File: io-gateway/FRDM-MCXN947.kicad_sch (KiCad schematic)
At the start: 12 parts, among them M1 Fan_3pin, U6 MCP9700x-ETT

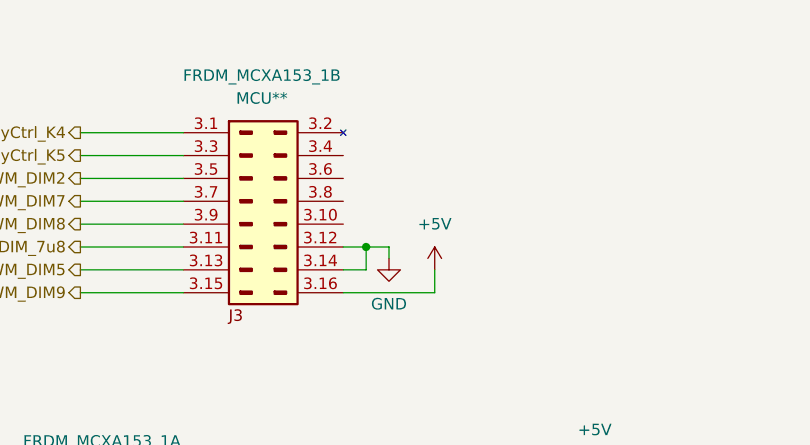
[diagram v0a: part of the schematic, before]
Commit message: Add ESD protection for RS485
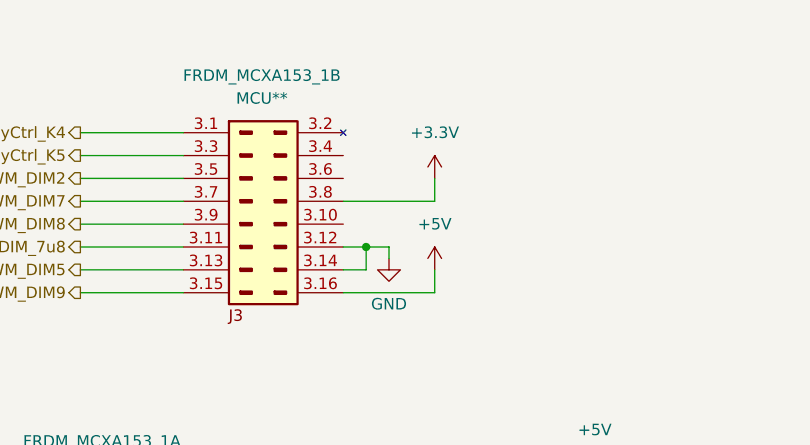
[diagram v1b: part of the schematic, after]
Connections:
- net +3.3V: now reaches FRDM_MCXA153_1.3.8 (Pin_J3_3V3_Out)
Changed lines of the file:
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@@
 	(wire
 		(pts
+			(xy 232.41 82.55) (xy 232.41 85.09)
+		)
+		(stroke
+			(width 0)
+			(type default)
+		)
+	)
+	(wire
+		(pts
 			(xy 266.7 116.84) (xy 250.19 116.84)
 		)
@@
 	(wire
 		(pts
+			(xy 232.41 85.09) (xy 222.25 85.09)
+		)
+		(stroke
+			(width 0)
+			(type default)
+		)
+	)
+	(wire
+		(pts
 			(xy 53.34 80.01) (xy 93.98 80.01)
 		)
@@
 				)
 			)
+		)
+	)
+	(symbol
+		(lib_id "power:+3.3V")
+		(at 232.41 82.55 0)
+		(unit 1)
+		(exclude_from_sim no)
+		(in_bom yes)
+		(on_board yes)
+		(dnp no)
+		(fields_autoplaced yes)
+		(property "Reference" "#PWR078"
+			(at 232.41 86.36 0)
+			(effects
+				(font
+					(size 1.27 1.27)
+				)
+				(hide yes)
+			)
+		)
+		(property "Value" "+3.3V"
+			(at 232.41 77.47 0)
+			(effects
+				(font
+					(size 1.27 1.27)
+				)
+			)
+		)
+		(property "Footprint" ""
+			(at 232.41 82.55 0)
+			(effects
+				(font
+					(size 1.27 1.27)
+				)
+				(hide yes)
+			)
+		)
+		(property "Datasheet" ""
+			(at 232.41 82.55 0)
+			(effects
+				(font
+					(size 1.27 1.27)
+				)
+				(hide yes)
+			)
+		)
+		(property "Description" "Power symbol creates a global label with name \"+3.3V\""
+			(at 232.41 82.55 0)
+			(effects
+				(font
+					(size 1.27 1.27)
+				)
+				(hide yes)
+			)
+		)
+		(pin "1"
+		)
+		(instances
+			(project ""
+				(path "/2cb6f94b-272a-4ed7-b08d-c3630bda6156/f7918fcf-9688-4ae8-a1d7-cb892536f0d4"
+					(reference "#PWR078")
+					(unit 1)
+				)
+			)

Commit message: upd
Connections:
- net RelayCtrl_K8: now also FRDM_MCXA153_1.4.9 (Pin_9); no longer FRDM_MCXA153_1.1.1 (Pin_J1_1)
- net RS485_RTS renamed RS485_DE
- new net RS_485_nRE: FRDM_MCXA153_1.1.1 (Pin_J1_1)
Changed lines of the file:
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@@
+	(wire
+		(pts
+			(xy 166.37 128.27) (xy 176.53 128.27)
+		)
+		(stroke
+			(width 0)
+			(type default)
+		)
+	)
 	(wire
 		(pts
@@
 	(wire
 		(pts
+			(xy 222.25 92.71) (xy 224.79 92.71)
+		)
+		(stroke
+			(width 0)
+			(type default)
+		)
+	)
+	(wire
+		(pts
+			(xy 250.19 133.35) (xy 250.19 135.89)
+		)
+		(stroke
+			(width 0)
+			(type default)
+		)
+	)
+	(wire
+		(pts
+			(xy 92.71 163.83) (xy 92.71 170.18)
+		)
+		(stroke
+			(width 0)
+			(type default)
+		)
+	)
+	(wire
+		(pts
+			(xy 125.73 90.17) (xy 128.27 90.17)
+		)
+		(stroke
+			(width 0)
+			(type default)
+		)
+	)
+	(wire
+		(pts
+			(xy 193.04 87.63) (xy 204.47 87.63)
+		)
+		(stroke
+			(width 0)
+			(type default)
+		)
+	)
+	(wire
+		(pts
+			(xy 40.64 144.78) (xy 40.64 142.24)
+		)
+		(stroke
+			(width 0)
+			(type default)
+		)
+	)
+	(wire
+		(pts
+			(xy 193.04 95.25) (xy 204.47 95.25)
+		)
+		(stroke
+			(width 0)
+			(type default)
+		)
+	)
+	(wire
+		(pts
+			(xy 76.2 95.25) (xy 93.98 95.25)
+		)
+		(stroke
+			(width 0)
+			(type default)
+		)
+	)
+	(wire
+		(pts
+			(xy 19.05 127) (xy 19.05 130.81)
+		)
+		(stroke
+			(width 0)
+			(type default)
+		)
+	)
+	(wire
+		(pts
+			(xy 19.05 144.78) (xy 40.64 144.78)
+		)
+		(stroke
+			(width 0)
+			(type default)
+		)
+	)
+	(wire
+		(pts
 			(xy 111.76 133.35) (xy 120.65 133.35)
-		)
-		(stroke
-			(width 0)
-			(type default)
-		)
-	)
-	(wire
-		(pts
-			(xy 222.25 92.71) (xy 224.79 92.71)
-		)
-		(stroke
-			(width 0)
-			(type default)
-		)
-	)
-	(wire
-		(pts
-			(xy 250.19 133.35) (xy 250.19 135.89)
-		)
-		(stroke
-			(width 0)
-			(type default)
-		)
-	)
-	(wire
-		(pts
-			(xy 92.71 163.83) (xy 92.71 170.18)
-		)
-		(stroke
-			(width 0)
-			(type default)
-		)
-	)
-	(wire
-		(pts
-			(xy 125.73 90.17) (xy 128.27 90.17)
-		)
-		(stroke
-			(width 0)
-			(type default)
-		)
-	)
-	(wire
-		(pts
-			(xy 193.04 87.63) (xy 204.47 87.63)
-		)
-		(stroke
-			(width 0)
-			(type default)
-		)
-	)
-	(wire
-		(pts
-			(xy 40.64 144.78) (xy 40.64 142.24)
-		)
-		(stroke
-			(width 0)
-			(type default)
-		)
-	)
-	(wire
-		(pts
-			(xy 193.04 95.25) (xy 204.47 95.25)
-		)
-		(stroke
-			(width 0)
-			(type default)
-		)
-	)
-	(wire
-		(pts
-			(xy 76.2 95.25) (xy 93.98 95.25)
-		)
-		(stroke
-			(width 0)
-			(type default)
-		)
-	)
-	(wire
-		(pts
-			(xy 19.05 127) (xy 19.05 130.81)
-		)
-		(stroke
-			(width 0)
-			(type default)
-		)
-	)
-	(wire
-		(pts
-			(xy 19.05 144.78) (xy 40.64 144.78)
 		)
 		(stroke
@@
 		)
 	)
-	(hierarchical_label "RS485_RTS"
+	(hierarchical_label "RS485_DE"
 		(shape output)
 		(at 120.65 130.81 0)
@@
 	(hierarchical_label "RelayCtrl_K8"
 		(shape output)
-		(at 120.65 133.35 0)
-		(effects
-			(font
-				(size 1.27 1.27)
-			)
-			(justify left)
+		(at 166.37 128.27 180)
+		(effects
+			(font
+				(size 1.27 1.27)
+			)
+			(justify right)
 		)
 	)
@@
 		)
 	)
+	(hierarchical_label "RS_485_nRE"
+		(shape output)
+		(at 120.65 133.35 0)
+		(effects
+			(font
+				(size 1.27 1.27)
+			)
+			(justify left)
+		)
+	)

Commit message: upd
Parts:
- added D5: SP1007-01ETG, Diode_SMD:D_SOD-882D, symbol Diode:PESD5V0L1ULD
- added R_F2: 10K, Resistor_SMD:R_0603_1608Metric_Pad0.98x0.95mm_HandSolder, symbol Device:R
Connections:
- net +5V: now also D5.1 (K)
- net GND: now also D5.2 (A), R_F2.2
- net at Q_F1.1 (G), R_F1.1: now also R_F2.1

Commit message: V1.2
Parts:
- C10, C11, R3, R4: value NM -> DNP
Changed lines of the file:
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@@
 			)
 		)
-		(property "Value" "NM"
+		(property "Value" "DNP"
 			(at 119.38 99.0599 0)
 			(effects
@@
 			)
 		)
-		(property "Value" "NM"
+		(property "Value" "DNP"
 			(at 123.19 83.82 90)
 			(effects
@@
 			)
 		)
-		(property "Value" "NM"
+		(property "Value" "DNP"
 			(at 132.08 86.36 90)
 			(effects
@@
 			)
 		)
-		(property "Value" "NM"
+		(property "Value" "DNP"
 			(at 129.54 99.0599 0)
 			(effects
